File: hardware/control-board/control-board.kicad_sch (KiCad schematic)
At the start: 233 parts, among them J1 XH-2A, J10 XH-2A, J11 XH-2A, J12 XH-2A, J13 XH-2A, J14 XH-2A, J15 XH-2A, J16 XH-2A, J17 XH-2A, J18 XH-2A, J19 XH-2A, J2 XH-2A, J20 XH-2A, J21 XH-2A, J22 XH-4A, J23 XH-4A, J24 XH-4A, J25 XH-4A, J26 XH-4A, J27 XH-4A, J28 XH-4A, J29 XH-2A, J3 XH-2A, J30 XH-2A, J31 XH-2A, J32 XH-2A, J33 XH-2A, J34 XH-2A, J35 XH-2A, J36 XH-2A, J37 XH-4A, J38 HB9500M-9.5-2P, J4 XH-2A, J5 XH-2A, J6 XH-2A, J7 XH-2A, J8 XH-2A, J9 XH-2A, Q1 AO3400A, Q10 AO3400A, Q11 AO3400A, Q12 AO3400A, Q2 AO3400A, Q3 AO3400A, Q4 AO3400A, Q5 AO3400A, Q6 AO3400A, Q7 AO3400A, Q8 AO3400A, Q9 AO3400A, SW1 TS-1187A-B-A-B, SW2 TS-1187A-B-A-B, T1 HX1188NL, U1 STM32H723ZGTx, U2 DP83825I, U3 TMC2209-LA, U4 TMC2209-LA, U5 XL1509-5.0, U6 AMS1117-3.3, U7 SN74LVC4245APWR, U8 W25Q128JVS, U9 TMI8340_C2985071, X1 X322525MOB4SI, X2 X322525MOB4SI, X3 Q13FC1350000400

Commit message: added indicator I/O, text labels
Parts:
- added C75, C76: 100nF 50V, Capacitor_SMD:C_0402_1005Metric, symbol Device:C_Small
- added J39: XH-4A, Connector_JST:JST_XH_B4B-XH-A_1x04_P2.50mm_Vertical, symbol Connector_Generic:Conn_01x04
- added R69: 10kR 1%, Resistor_SMD:R_0402_1005Metric, symbol Device:R
- added R70: 33kR 1%, Resistor_SMD:R_0402_1005Metric, symbol Device:R
- added U10: LM393, Package_SO:SOIC-8_3.9x4.9mm_P1.27mm, symbol Comparator:LM393
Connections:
- net +3.3V: now also C76.2, R70.1, U10.8 (V+)
- net GND: now also C75.1, C76.1, J39.1 (Pin_1), J39.2 (Pin_2), R69.2, U10.4 (V-)
- net INDICATOR_DATA: now reaches U1.66 (PE13)
- net INDICATOR_DATA: now also U10.1
- net INDICATOR_CLK: now reaches U1.67 (PE14)
- net INDICATOR_CLK: now also U10.7
- new net INDICATOR_CLK_IN: J39.4 (Pin_4), U10.5 (+)
- new net INDICATOR_DATA_IN: J39.3 (Pin_3), U10.3 (+)
- new net INDICATOR_VREF: C75.2, R69.1, R70.2, U10.2 (-), U10.6 (-)
- no-connect marks 57 -> 55
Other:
- moved on the sheet: J37, J38

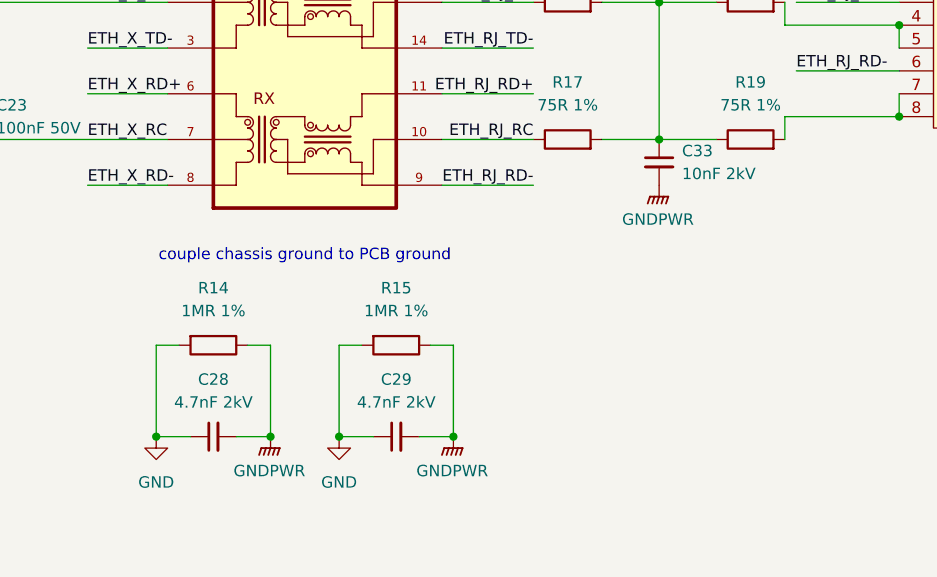
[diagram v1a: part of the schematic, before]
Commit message: changed ethernet termination capacitors to 1nF
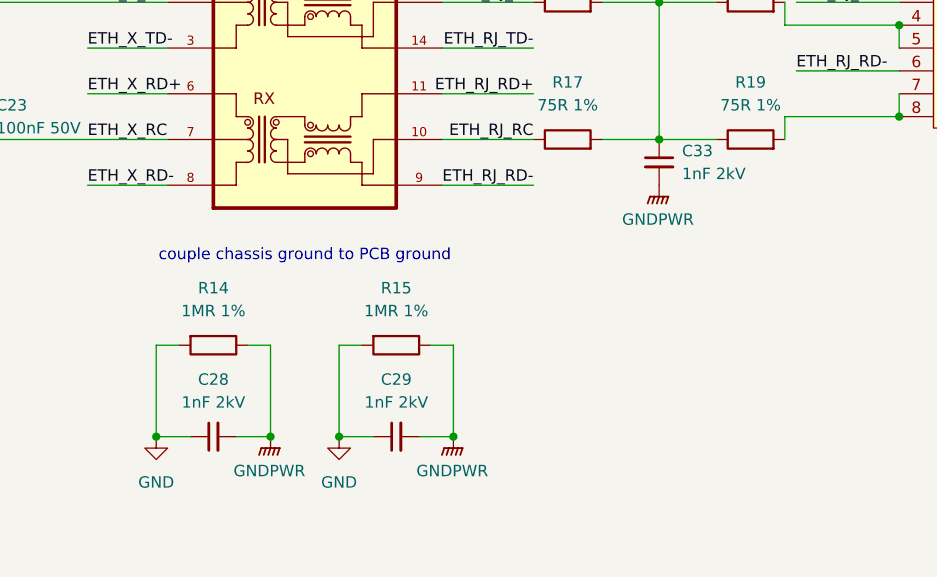
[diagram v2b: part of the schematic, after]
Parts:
- C28, C29: value 4.7nF 2kV -> 1nF 2kV
- C33: value 10nF 2kV -> 1nF 2kV
